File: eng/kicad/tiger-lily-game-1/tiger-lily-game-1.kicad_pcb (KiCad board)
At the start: 2 copper layers, 11 parts, among them J1 Conn_01x06_Male, SW1 SW_Push, SW2 SW_Push, SW3 SW_Push, SW4 SW_SPDT, U1 PIC16F1454-IP

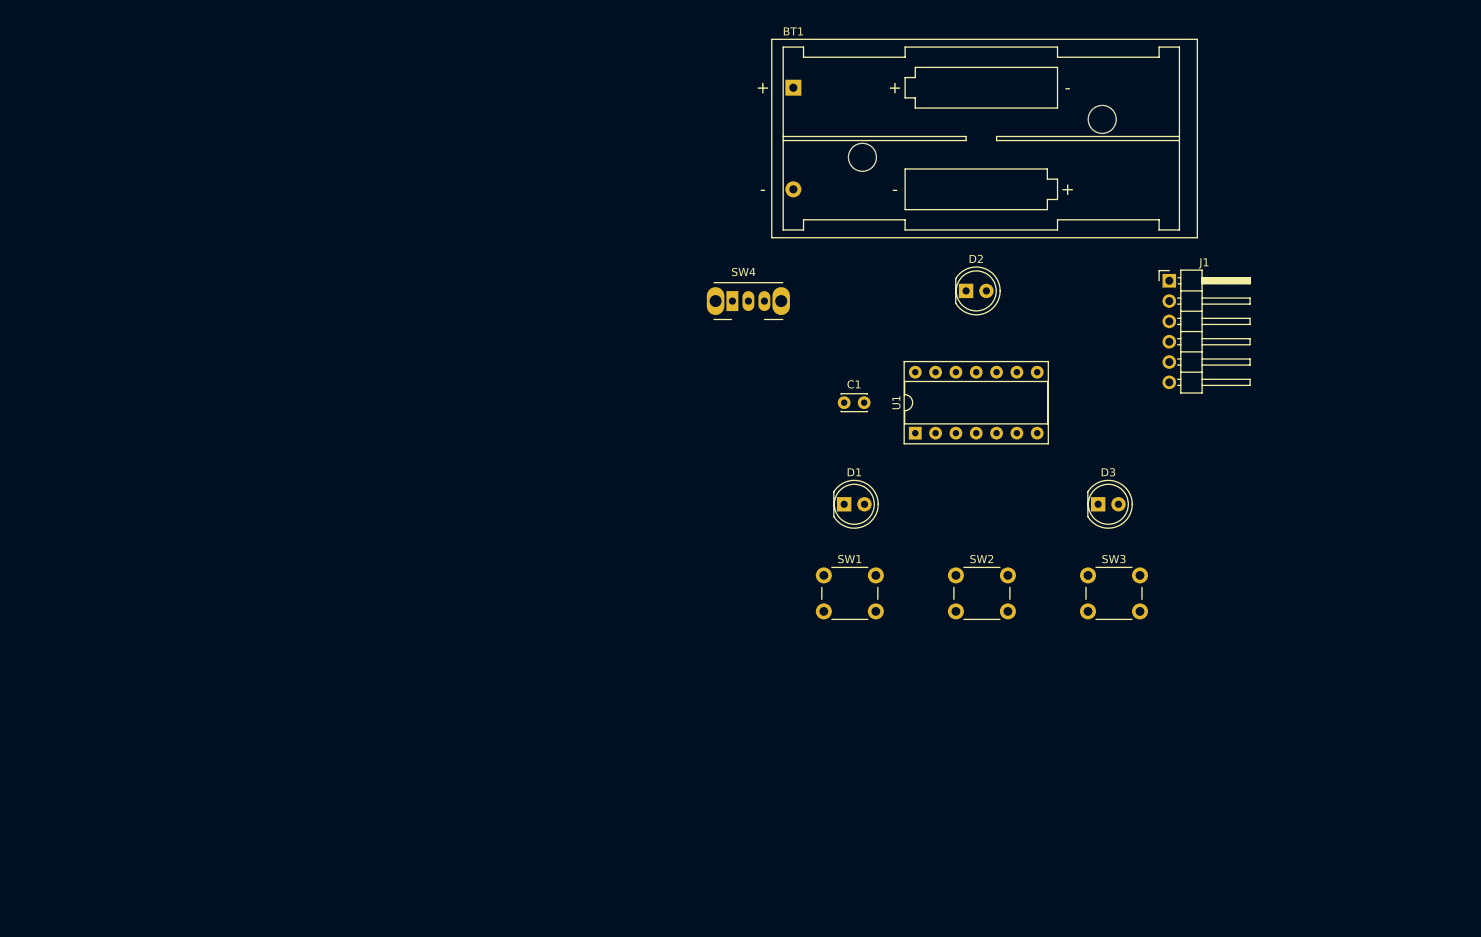
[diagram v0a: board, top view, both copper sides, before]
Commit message: Changed MCU to PIC16F15323 as simpler, cheaper, and available. Added custom schematic for MCU as not in library installed. Tried PCB layout (do not like it so will change). Added skeleton firmware project files.
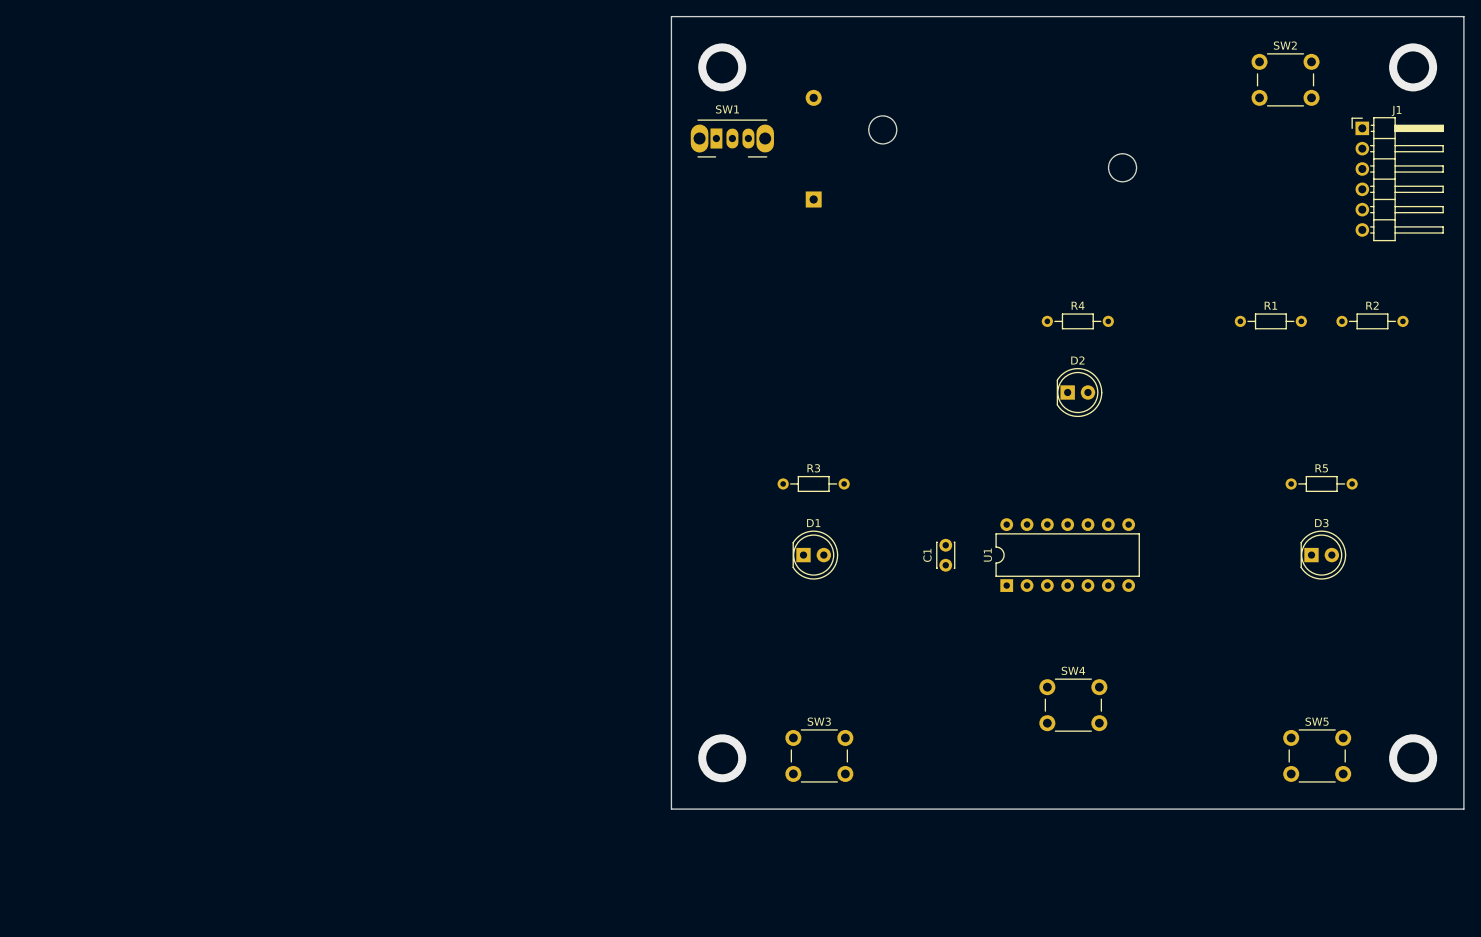
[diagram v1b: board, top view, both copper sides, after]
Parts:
- added R1: 10K, Resistor_THT:R_Axial_DIN0204_L3.6mm_D1.6mm_P7.62mm_Horizontal, F.Cu at (242.6, 76.2)
- added R2: 1K, Resistor_THT:R_Axial_DIN0204_L3.6mm_D1.6mm_P7.62mm_Horizontal, F.Cu at (255.3, 76.2)
- added R3: 330R, Resistor_THT:R_Axial_DIN0204_L3.6mm_D1.6mm_P7.62mm_Horizontal, F.Cu at (185.4, 96.5)
- added R4: 330R, Resistor_THT:R_Axial_DIN0204_L3.6mm_D1.6mm_P7.62mm_Horizontal, F.Cu at (218.4, 76.2)
- added R5: 330R, Resistor_THT:R_Axial_DIN0204_L3.6mm_D1.6mm_P7.62mm_Horizontal, F.Cu at (248.9, 96.5)
- added SW5: SW_P2, Button_Switch_THT:SW_PUSH_6mm, F.Cu at (248.9, 128.3)
- BT1: moved to B.Cu
- C1: value C -> 0.1uF
- SW1: value SW_Push -> SW_PWR; footprint Button_Switch_THT:SW_PUSH_6mm -> Button_Switch_THT:SW_CuK_OS102011MA1QN1_SPDT_Angled
- SW2: value SW_Push -> SW_RESET
- SW3: value SW_Push -> SW_P1
- SW4: value SW_SPDT -> SW_PLAY; footprint Button_Switch_THT:SW_CuK_OS102011MA1QN1_SPDT_Angled -> Button_Switch_THT:SW_PUSH_6mm
- U1: value PIC16F1454-IP -> PIC16F15323-IP; footprint Package_DIP:DIP-14_W7.62mm_Socket -> Package_DIP:DIP-14_W7.62mm
- moved SW2 74.6 mm to (245.0, 43.8)
- moved SW4 62.3 mm to (218.4, 121.9)
- moved SW1 56.2 mm to (177.1, 53.3)
- moved SW3 42.1 mm to (186.7, 128.3)
- moved J1 30.7 mm to (257.8, 52.1)
- moved D3 27.4 mm to (251.5, 105.4)
- moved C1 24.0 mm to (205.7, 106.7), turned to 90 degrees
- moved U1 22.2 mm to (213.4, 109.2)
- moved D2 18.0 mm to (221.0, 85.1)
- moved BT1 14.2 mm to (189.2, 61.0)
- moved D1 8.13 mm to (188.0, 105.4)
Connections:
- BT1 pad 1: (no net) -> Net-(BT1-Pad1)
- BT1 pad 2: (no net) -> /MCU_GND
- C1 pad 1: (no net) -> /MCU_PWR
- C1 pad 2: (no net) -> /MCU_GND
- J1 pad 2: (no net) -> /MCU_PWR
- J1 pad 3: (no net) -> /MCU_GND
- SW1 pad 2: Net-(SW1-Pad2) -> Net-(BT1-Pad1)
- SW4 pad 1: (no net) -> Net-(SW4-Pad1)
- SW4 pad 2: (no net) -> Net-(SW4-Pad2)
- U1 pad 1: (no net) -> /MCU_PWR
- U1 pad 14: (no net) -> /MCU_GND
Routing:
- net (no net): vias 0 -> 4
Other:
- board outline added: 99.1 x 99.1 mm

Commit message: Schematic and PCB design (WIP). Firmware (WIP). Checked in for backup.
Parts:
- added G***: LOGO, tiger-lily-logo:tiger-lily-logo-160, F.Cu at (111.8, 91.4)
- added R6: 330R, Resistor_THT:R_Axial_DIN0204_L3.6mm_D1.6mm_P7.62mm_Horizontal, F.Cu at (105.4, 134.6)
- added R7: 330R, Resistor_THT:R_Axial_DIN0204_L3.6mm_D1.6mm_P7.62mm_Horizontal, F.Cu at (135.9, 134.6)
- added R8: 330R, Resistor_THT:R_Axial_DIN0204_L3.6mm_D1.6mm_P7.62mm_Horizontal, F.Cu at (167.6, 134.6)
- BT1: moved to F.Cu
- moved SW2 95.6 mm to (160.0, 87.6)
- moved R2 85.9 mm to (170.2, 64.8), turned to 90 degrees
- moved SW4 85.0 mm to (135.9, 142.2)
- moved R4 83.0 mm to (135.9, 85.1)
- moved D2 83.0 mm to (138.4, 94.0)
- moved D1 82.5 mm to (106.7, 119.4)
- moved D3 82.5 mm to (170.2, 119.4)
- moved R5 82.5 mm to (167.6, 110.5)
- moved SW3 82.5 mm to (105.4, 142.2)
- moved SW5 82.5 mm to (167.6, 142.2)
- moved R3 82.5 mm to (104.1, 110.5)
- moved J1 81.0 mm to (177.8, 64.8)
- moved R1 78.3 mm to (167.6, 99.1), turned to 180 degrees
- moved U1 78.1 mm to (135.3, 111.8), turned to 0 degrees
- moved SW1 77.7 mm to (101.6, 71.7), turned to 270 degrees
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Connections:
- D1 pad 1: (no net) -> /LED_P1
- D1 pad 2: (no net) -> Net-(D1-Pad2)
- D2 pad 1: (no net) -> /LED_GO
- D2 pad 2: (no net) -> Net-(D2-Pad2)
- D3 pad 1: (no net) -> /LED_P2
- D3 pad 2: (no net) -> Net-(D3-Pad2)
- J1 pad 1: (no net) -> /MCU_VPP
- J1 pad 4: (no net) -> /MCU_ICSPXXX
- J1 pad 5: (no net) -> /MCU_ICSPYYY
- J1 pad 6: (no net) -> Net-(J1-Pad6)
- R1 pad 1: (no net) -> /MCU_PWR
- R1 pad 2: (no net) -> Net-(R1-Pad2)
- R2 pad 1: (no net) -> /MCU_VPP
- R2 pad 2: (no net) -> Net-(R1-Pad2)
- R3 pad 1: (no net) -> /MCU_PWR
- R3 pad 2: (no net) -> Net-(D1-Pad2)
- R4 pad 1: (no net) -> /MCU_PWR
- R4 pad 2: (no net) -> Net-(D2-Pad2)
- R5 pad 1: (no net) -> /MCU_PWR
- R5 pad 2: (no net) -> Net-(D3-Pad2)
- SW2 pad 1: Net-(SW2-Pad1) -> /MCU_GND
- SW2 pad 2: Net-(SW2-Pad2) -> Net-(R1-Pad2)
- SW3 pad 2: Net-(SW3-Pad2) -> /SW_P1
- SW4 pad 2: Net-(SW4-Pad2) -> /SW_GO
- SW5 pad 2: Net-(SW5-Pad2) -> /SW_P2
- U1 pad 10: (no net) -> /LED_P1
- U1 pad 11: (no net) -> Net-(U1-Pad11)
- U1 pad 12: (no net) -> /MCU_ICSPYYY
- U1 pad 13: (no net) -> /MCU_ICSPXXX
- U1 pad 2: (no net) -> Net-(U1-Pad2)
- U1 pad 3: (no net) -> Net-(U1-Pad3)
- U1 pad 4: (no net) -> /MCU_VPP
- U1 pad 5: (no net) -> /SW_P2
- U1 pad 6: (no net) -> /SW_GO
- U1 pad 7: (no net) -> /SW_P1
- U1 pad 8: (no net) -> /LED_P2
- U1 pad 9: (no net) -> /LED_GO
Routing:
- net /MCU_PWR: track 0.00 -> 110.4 mm
- net /MCU_GND: track 0.00 -> 104.5 mm
- net /MCU_VPP: track 0.00 -> 76.7 mm
- net Net-(R1-Pad2): track 0.00 -> 53.2 mm
- net /SW_P2: track 0.00 -> 49.1 mm
- net /SW_P1: track 0.00 -> 38.0 mm
- net /LED_P1: track 0.00 -> 38.0 mm
- net /LED_GO: track 0.00 -> 35.0 mm
- net /SW_GO: track 0.00 -> 31.1 mm
- net /LED_P2: track 0.00 -> 30.4 mm
- net Net-(BT1-Pad1): track 0.00 -> 20.0 mm
- net Net-(R8-Pad1): track 0.00 -> 14.1 mm
- net Net-(R7-Pad1): track 0.00 -> 14.1 mm
- net Net-(R6-Pad1): track 0.00 -> 14.1 mm
- net Net-(D1-Pad2): track 0.00 -> 9.94 mm
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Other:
- board text added: "Reaction Game Copyright (C) 2021 Tiger-Lily"

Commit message: Candidate Schematic and PCB. TODO: Check silkscreen text.
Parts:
- BT1: footprint Battery:BatteryHolder_Keystone_2468_2xAAA -> Battery:BatteryHolder_Keystone_2479_3xAAA
- moved R2 25.4 mm to (171.4, 90.2), turned to 270 degrees
- moved D2 25.4 mm to (138.4, 119.4)
- moved R4 25.4 mm to (135.9, 110.5)
- moved R1 17.8 mm to (185.4, 97.8)
- moved SW2 17.8 mm to (177.8, 86.4)
- moved C1 11.8 mm to (126.3, 101.9), turned to 90 degrees
- moved G*** 10.9 mm to (102.9, 85.1)
- moved U1 7.51 mm to (133.9, 104.4), turned to 90 degrees
- moved SW1 4.35 mm to (101.6, 67.3)
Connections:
- U1 pad 5: /SW_P2 -> /SW_P1
- U1 pad 7: /SW_P1 -> /SW_P2
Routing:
- net /MCU_GND: track 104.5 -> 231.8 mm
- net /MCU_PWR: track 110.4 -> 179.1 mm
- net /MCU_ICSPXXX: track 0.00 -> 51.5 mm
- net /MCU_ICSPYYY: track 0.00 -> 47.9 mm
- net Net-(R1-Pad2): track 53.2 -> 19.8 mm
- net /SW_P1: track 38.0 -> 62.1 mm
- net /SW_GO: track 31.1 -> 50.6 mm
- net /LED_P1: track 38.0 -> 47.4 mm
- net /MCU_VPP: track 76.7 -> 67.3 mm
- net /LED_GO: track 35.0 -> 26.0 mm
- net /SW_P2: track 49.1 -> 56.5 mm
- net (no net): track 0.00 -> 2.52 mm
- net Net-(BT1-Pad1): track 20.0 -> 18.7 mm
- net /LED_P2: track 30.4 -> 31.3 mm
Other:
- board text added: "Reaction Game Copyright (C) 2021 Tiger-Lily Version 1.0"
- board text removed: "Reaction Game Copyright (C) 2021 Tiger-Lily"
